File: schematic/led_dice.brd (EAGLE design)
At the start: 39.4 x 64.8 mm, 13 parts, among them IC1 74HC595N, U1 ATTINY85-20P

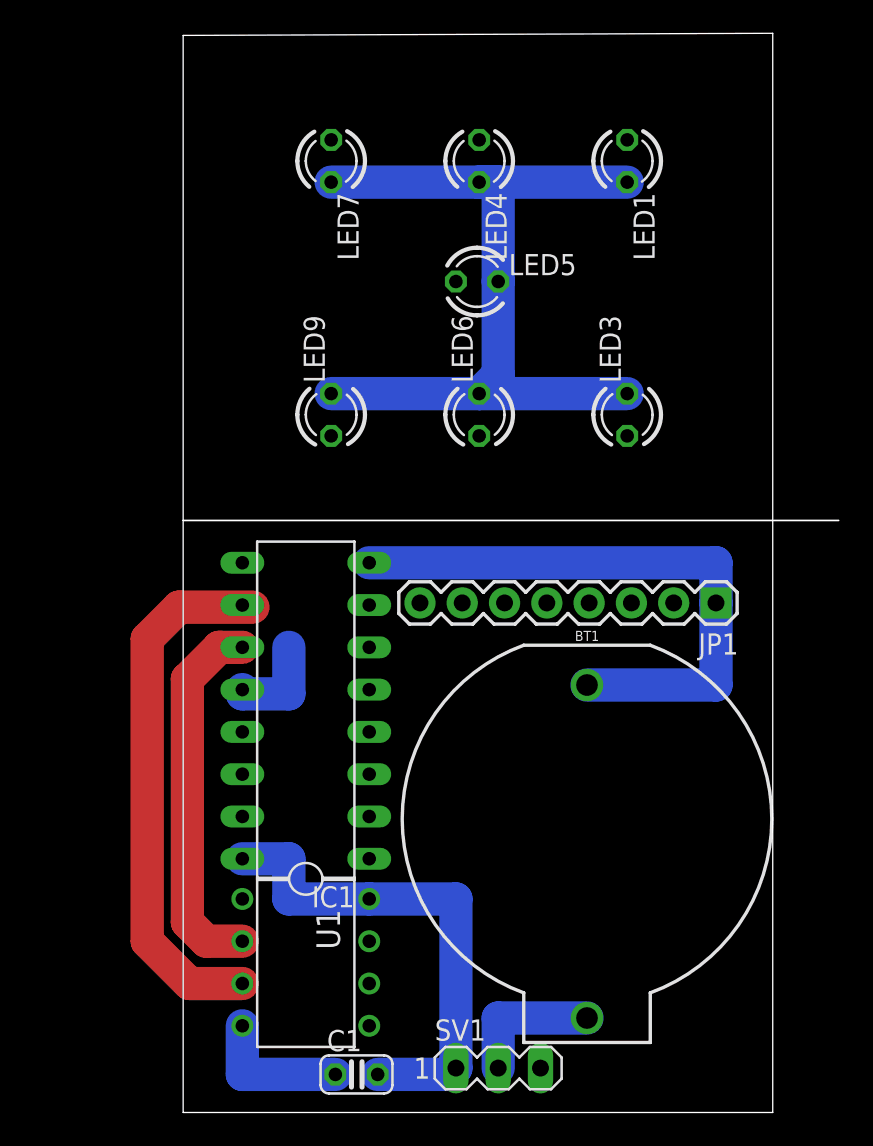
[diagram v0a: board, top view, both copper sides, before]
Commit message: Schematic fixes
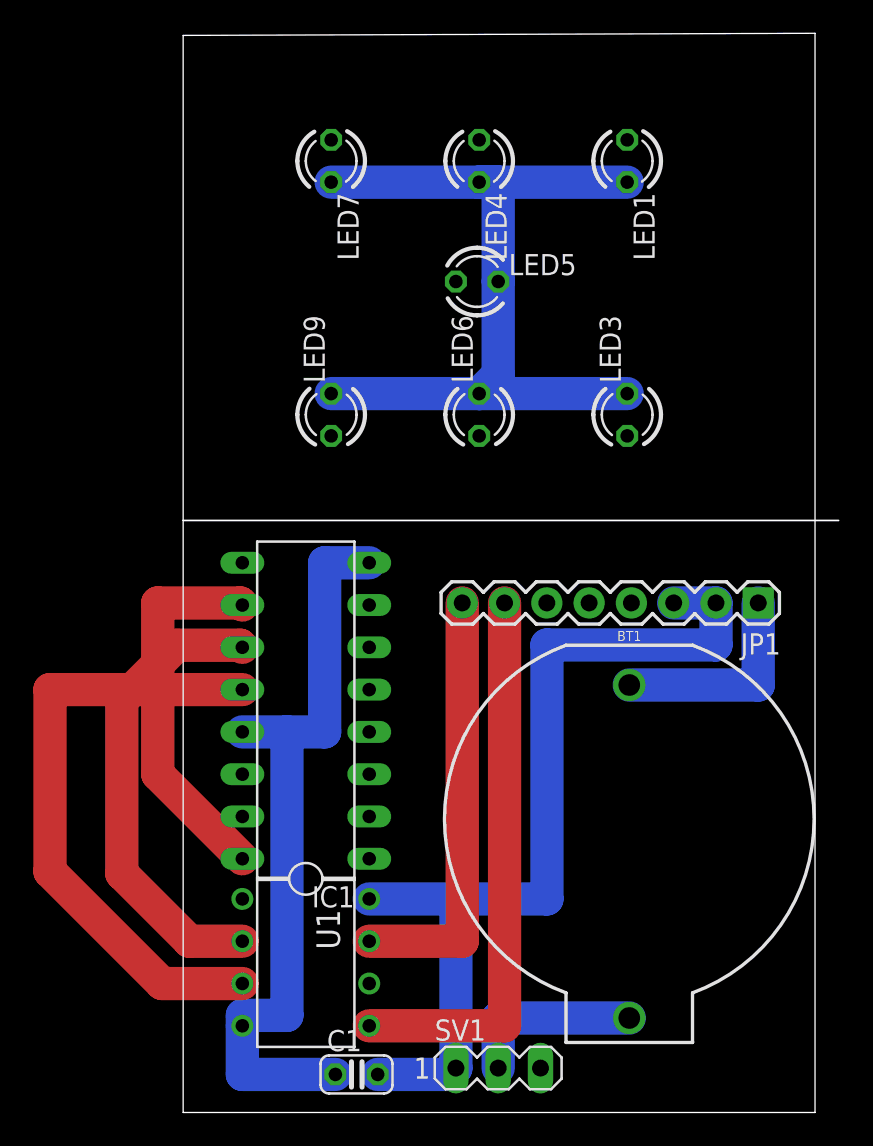
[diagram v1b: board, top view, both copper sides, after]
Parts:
- moved BT1 2.54 mm to (26.8, 11.2)
- moved JP1 2.54 mm to (34.5, 24.3)
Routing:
- net VCC: track 30.3 -> 78.8 mm
- net SDA: track 0.00 -> 33.5 mm
- net SCL: track 0.00 -> 25.9 mm
- net GND: track 94.3 -> 109.2 mm
- net N$4: track 22.5 -> 28.0 mm
- net N$6: track 8.34 -> 10.9 mm
- net N$8: track 37.9 -> 36.8 mm
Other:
- outline, holes or cut-outs redrawn

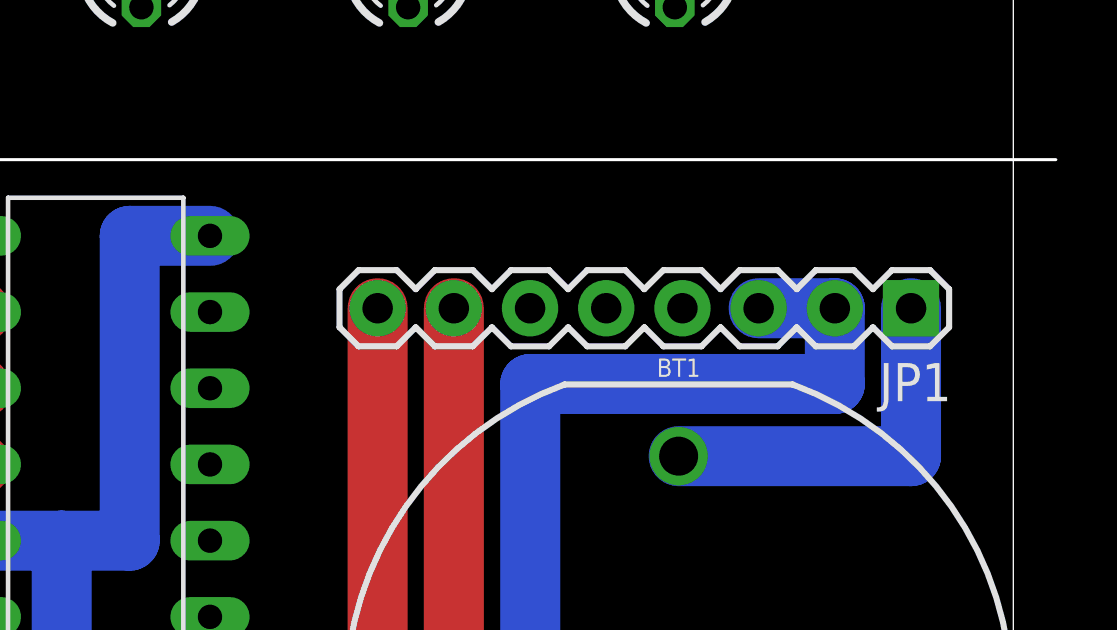
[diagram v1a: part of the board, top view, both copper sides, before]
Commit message: Sketch: added Shuffle Effect + 3d case updated
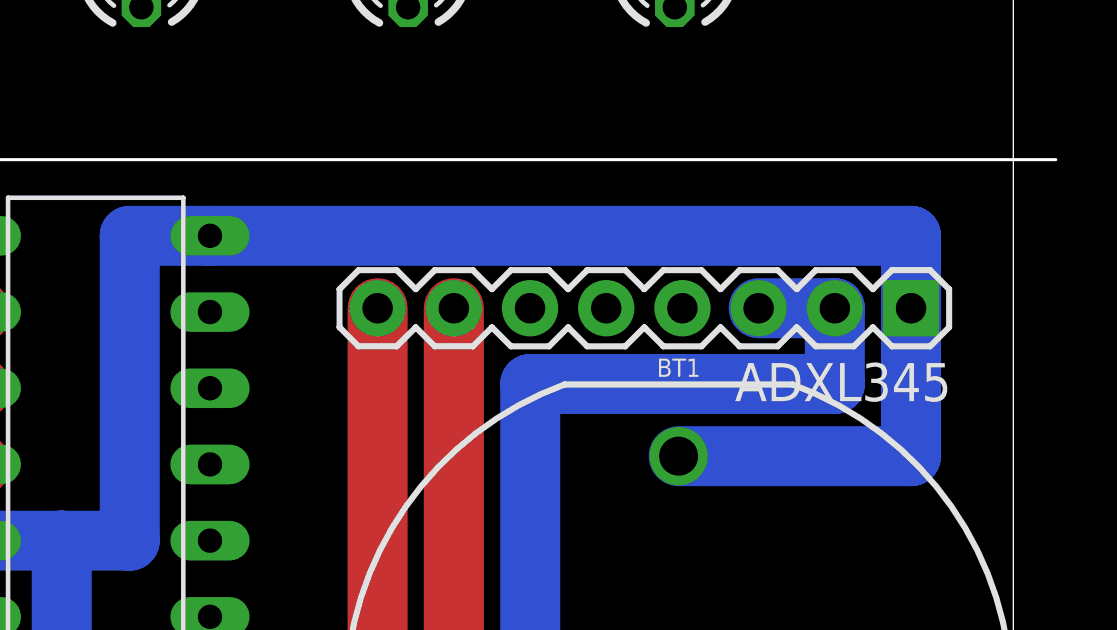
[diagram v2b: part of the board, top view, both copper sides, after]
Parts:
- renumbered JP1 to ADXL345
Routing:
- net GND: track 109.2 -> 135.0 mm
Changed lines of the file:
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@@
 <attribute name="VALUE" x="26.797" y="11.176" size="0.6096" layer="27" font="vector" ratio="20" align="top-center"/>
 </element>
-<element name="JP1" library="SparkFun" package="1X08" value="" x="34.544" y="24.257" smashed="yes" rot="R180">
+<element name="ADXL345" library="SparkFun" package="1X08" value="" x="34.544" y="24.257" smashed="yes" rot="R180">
 <attribute name="NAME" x="35.8902" y="22.4282" size="1.27" layer="25" ratio="10" rot="R180"/>
 <attribute name="VALUE" x="35.814" y="27.432" size="1.27" layer="27" rot="R180"/>
@@
 <signals>
 <signal name="GND">
-<contactref element="JP1" pad="1"/>
+<contactref element="ADXL345" pad="1"/>
 <contactref element="U1" pad="4"/>
 <contactref element="BT1" pad="2"/>
@@
 <wire x1="17.78" y1="49.53" x2="26.67" y2="49.53" width="2" layer="16"/>
 <wire x1="26.797" y1="19.326" x2="34.544" y2="19.326" width="2" layer="16"/>
-<wire x1="34.544" y1="19.326" x2="32.004" y2="20.32" width="0" layer="19" extent="1-16"/>
 <wire x1="34.544" y1="19.326" x2="34.544" y2="24.257" width="2" layer="16"/>
 <wire x1="3.556" y1="-1.143" x2="3.556" y2="-0.5174" width="2" layer="16"/>
@@
 <wire x1="8.4996" y1="26.67" x2="8.4996" y2="16.51" width="2" layer="16"/>
 <wire x1="8.4996" y1="16.51" x2="6.223" y2="16.51" width="2" layer="16"/>
-<wire x1="3.556" y1="16.51" x2="8.89" y2="36.83" width="0" layer="19" extent="1-1"/>
-<wire x1="32.004" y1="20.32" x2="26.67" y2="36.83" width="0" layer="19" extent="1-1"/>
+<wire x1="34.544" y1="24.257" x2="34.544" y2="26.67" width="2" layer="16"/>
+<wire x1="34.544" y1="26.67" x2="11.176" y2="26.67" width="2" layer="16"/>
+<wire x1="11.176" y1="26.67" x2="8.89" y2="36.83" width="0" layer="19" extent="1-1"/>
 </signal>
 <signal name="INT2">
-<contactref element="JP1" pad="5"/>
+<contactref element="ADXL345" pad="5"/>
 </signal>
 <signal name="INT1">
-<contactref element="JP1" pad="4"/>
+<contactref element="ADXL345" pad="4"/>
 </signal>
 <signal name="VCC">
@@
 <contactref element="C1" pad="2"/>
 <contactref element="IC1" pad="10"/>
-<contactref element="JP1" pad="2"/>
-<contactref element="JP1" pad="3"/>
+<contactref element="ADXL345" pad="2"/>
+<contactref element="ADXL345" pad="3"/>
 <wire x1="16.383" y1="-3.683" x2="16.002" y2="-4.064" width="2" layer="16"/>
 <wire x1="16.002" y1="-4.064" x2="11.684" y2="-4.064" width="2" layer="16"/>
@@
 </signal>
 <signal name="SCL">
-<contactref element="JP1" pad="8"/>
+<contactref element="ADXL345" pad="8"/>
 <contactref element="U1" pad="7"/>
 <wire x1="11.176" y1="3.937" x2="16.764" y2="3.937" width="2" layer="1"/>
@@
 </signal>
 <signal name="SDA">
-<contactref element="JP1" pad="7"/>
+<contactref element="ADXL345" pad="7"/>
 <contactref element="U1" pad="5"/>
 <wire x1="11.176" y1="-1.143" x2="19.304" y2="-1.143" width="2" layer="1"/>
@@
 </signal>
 <signal name="N$10">
-<contactref element="JP1" pad="6"/>
+<contactref element="ADXL345" pad="6"/>
 </signal>
 <signal name="N$6">
